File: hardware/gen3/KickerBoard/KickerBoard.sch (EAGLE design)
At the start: 109 parts, among them U2 ATMEGA165PV-8AU

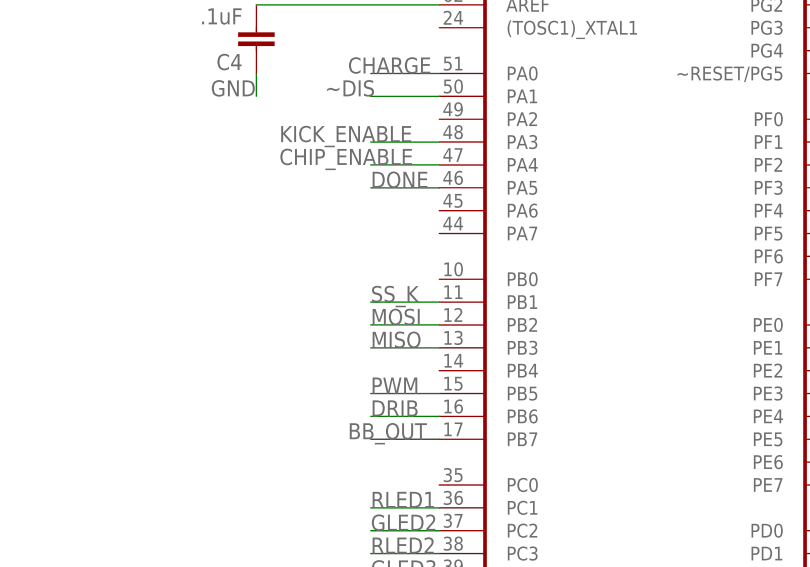
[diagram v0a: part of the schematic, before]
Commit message: fixed slave select issues
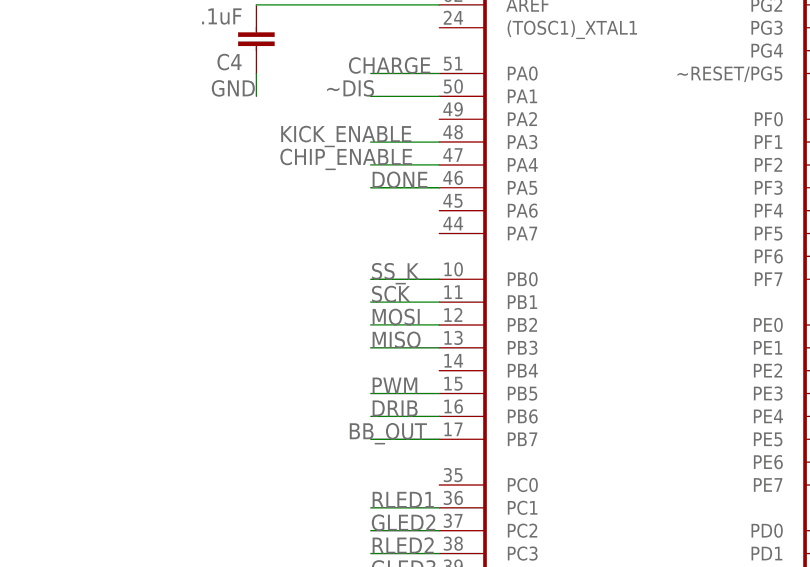
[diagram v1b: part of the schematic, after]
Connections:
- net SCK: now also U2.PB1
- net SS_K: now also U2.PB0; no longer U2.PB1
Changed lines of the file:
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@@
 <?xml version="1.0" encoding="utf-8"?>
 <!DOCTYPE eagle SYSTEM "eagle.dtd">
-<eagle version="6.4">
+<eagle version="7.2.0">
 <drawing>
 <settings>
@@
 <grid distance="0.1" unitdist="inch" unit="inch" style="lines" multiple="1" display="no" altdistance="0.01" altunitdist="inch" altunit="inch"/>
 <layers>
-<layer number="1" name="Top" color="4" fill="1" visible="yes" active="no"/>
-<layer number="2" name="Route2" color="1" fill="3" visible="yes" active="no"/>
-<layer number="3" name="Route3" color="4" fill="3" visible="yes" active="no"/>
-<layer number="14" name="Route14" color="1" fill="6" visible="yes" active="no"/>
-<layer number="15" name="Route15" color="4" fill="6" visible="yes" active="no"/>
-<layer number="16" name="Bottom" color="1" fill="1" visible="yes" active="no"/>
-<layer number="17" name="Pads" color="2" fill="1" visible="yes" active="no"/>
-<layer number="18" name="Vias" color="2" fill="1" visible="yes" active="no"/>
-<layer number="19" name="Unrouted" color="6" fill="1" visible="yes" active="no"/>
-<layer number="20" name="Dimension" color="15" fill="1" visible="yes" active="no"/>
-<layer number="21" name="tPlace" color="16" fill="1" visible="yes" active="no"/>
-<layer number="22" name="bPlace" color="14" fill="1" visible="yes" active="no"/>
-<layer number="23" name="tOrigins" color="15" fill="1" visible="yes" active="no"/>
-<layer number="24" name="bOrigins" color="15" fill="1" visible="yes" active="no"/>
-<layer number="25" name="tNames" color="7" fill="1" visible="yes" active="no"/>
-<layer number="26" name="bNames" color="7" fill="1" visible="yes" active="no"/>
-<layer number="27" name="tValues" color="7" fill="1" visible="yes" active="no"/>
-<layer number="28" name="bValues" color="7" fill="1" visible="yes" active="no"/>
+<layer number="1" name="Top" color="4" fill="1" visible="no" active="no"/>
+<layer number="2" name="Route2" color="1" fill="3" visible="no" active="no"/>
+<layer number="3" name="Route3" color="4" fill="3" visible="no" active="no"/>
+<layer number="14" name="Route14" color="1" fill="6" visible="no" active="no"/>
+<layer number="15" name="Route15" color="4" fill="6" visible="no" active="no"/>
+<layer number="16" name="Bottom" color="1" fill="1" visible="no" active="no"/>
+<layer number="17" name="Pads" color="2" fill="1" visible="no" active="no"/>
+<layer number="18" name="Vias" color="2" fill="1" visible="no" active="no"/>
+<layer number="19" name="Unrouted" color="6" fill="1" visible="no" active="no"/>
+<layer number="20" name="Dimension" color="15" fill="1" visible="no" active="no"/>
+<layer number="21" name="tPlace" color="16" fill="1" visible="no" active="no"/>
+<layer number="22" name="bPlace" color="14" fill="1" visible="no" active="no"/>
+<layer number="23" name="tOrigins" color="15" fill="1" visible="no" active="no"/>
+<layer number="24" name="bOrigins" color="15" fill="1" visible="no" active="no"/>
+<layer number="25" name="tNames" color="7" fill="1" visible="no" active="no"/>
+<layer number="26" name="bNames" color="7" fill="1" visible="no" active="no"/>
+<layer number="27" name="tValues" color="7" fill="1" visible="no" active="no"/>
+<layer number="28" name="bValues" color="7" fill="1" visible="no" active="no"/>
 <layer number="29" name="tStop" color="7" fill="3" visible="no" active="no"/>
 <layer number="30" name="bStop" color="7" fill="6" visible="no" active="no"/>
@@
 <layer number="35" name="tGlue" color="7" fill="4" visible="no" active="no"/>
 <layer number="36" name="bGlue" color="7" fill="5" visible="no" active="no"/>
-<layer number="37" name="tTest" color="7" fill="1" visible="yes" active="no"/>
-<layer number="38" name="bTest" color="7" fill="1" visible="yes" active="no"/>
+<layer number="37" name="tTest" color="7" fill="1" visible="no" active="no"/>
+<layer number="38" name="bTest" color="7" fill="1" visible="no" active="no"/>
 <layer number="39" name="tKeepout" color="4" fill="11" visible="no" active="no"/>
 <layer number="40" name="bKeepout" color="1" fill="11" visible="no" active="no"/>
@@
 <layer number="44" name="Drills" color="7" fill="1" visible="no" active="no"/>
 <layer number="45" name="Holes" color="7" fill="1" visible="no" active="no"/>
-<layer number="46" name="Milling" color="3" fill="1" visible="yes" active="no"/>
-<layer number="47" name="Measures" color="7" fill="1" visible="yes" active="no"/>
-<layer number="48" name="Document" color="7" fill="1" visible="yes" active="no"/>
-<layer number="49" name="Reference" color="7" fill="1" visible="yes" active="no"/>
-<layer number="50" name="dxf" color="7" fill="1" visible="yes" active="no"/>
-<layer number="51" name="tDocu" color="6" fill="1" visible="yes" active="no"/>
-<layer number="52" name="bDocu" color="7" fill="1" visible="yes" active="no"/>
-<layer number="53" name="tGND_GNDA" color="7" fill="9" visible="yes" active="no"/>
-<layer number="54" name="bGND_GNDA" color="1" fill="9" visible="yes" active="no"/>
-<layer number="56" name="wert" color="7" fill="1" visible="yes" active="no"/>
-<layer number="57" name="tCAD" color="7" fill="1" visible="yes" active="no"/>
-<layer number="59" name="tCarbon" color="7" fill="1" visible="yes" active="no"/>
-<layer number="60" name="bCarbon" color="7" fill="1" visible="yes" active="no"/>
+<layer number="46" name="Milling" color="3" fill="1" visible="no" active="no"/>
+<layer number="47" name="Measures" color="7" fill="1" visible="no" active="no"/>
+<layer number="48" name="Document" color="7" fill="1" visible="no" active="no"/>
+<layer number="49" name="Reference" color="7" fill="1" visible="no" active="no"/>
+<layer number="50" name="dxf" color="7" fill="1" visible="no" active="no"/>
+<layer number="51" name="tDocu" color="6" fill="1" visible="no" active="no"/>
+<layer number="52" name="bDocu" color="7" fill="1" visible="no" active="no"/>
+<layer number="53" name="tGND_GNDA" color="7" fill="9" visible="no" active="no"/>
+<layer number="54" name="bGND_GNDA" color="1" fill="9" visible="no" active="no"/>
+<layer number="56" name="wert" color="7" fill="1" visible="no" active="no"/>
+<layer number="57" name="tCAD" color="7" fill="1" visible="no" active="no"/>
+<layer number="59" name="tCarbon" color="7" fill="1" visible="no" active="no"/>
+<layer number="60" name="bCarbon" color="7" fill="1" visible="no" active="no"/>
 <layer number="90" name="Modules" color="5" fill="1" visible="yes" active="yes"/>
 <layer number="91" name="Nets" color="2" fill="1" visible="yes" active="yes"/>
@@
 <label x="55.88" y="35.56" size="1.778" layer="95"/>
 </segment>
+<segment>
+<pinref part="U2" gate="A" pin="PB1"/>
+<wire x1="101.6" y1="114.3" x2="93.98" y2="114.3" width="0.1524" layer="91"/>
+<label x="93.98" y="114.3" size="1.778" layer="95"/>
+</segment>
 </net>
 <net name="SS_M" class="0">
@@
 </segment>
 <segment>
-<pinref part="U2" gate="A" pin="PB1"/>
-<wire x1="101.6" y1="114.3" x2="93.98" y2="114.3" width="0.1524" layer="91"/>
-<label x="93.98" y="114.3" size="1.778" layer="95"/>
+<pinref part="U2" gate="A" pin="PB0"/>
+<wire x1="101.6" y1="116.84" x2="93.98" y2="116.84" width="0.1524" layer="91"/>
+<label x="93.98" y="116.84" size="1.778" layer="95"/>
 </segment>
 </net>

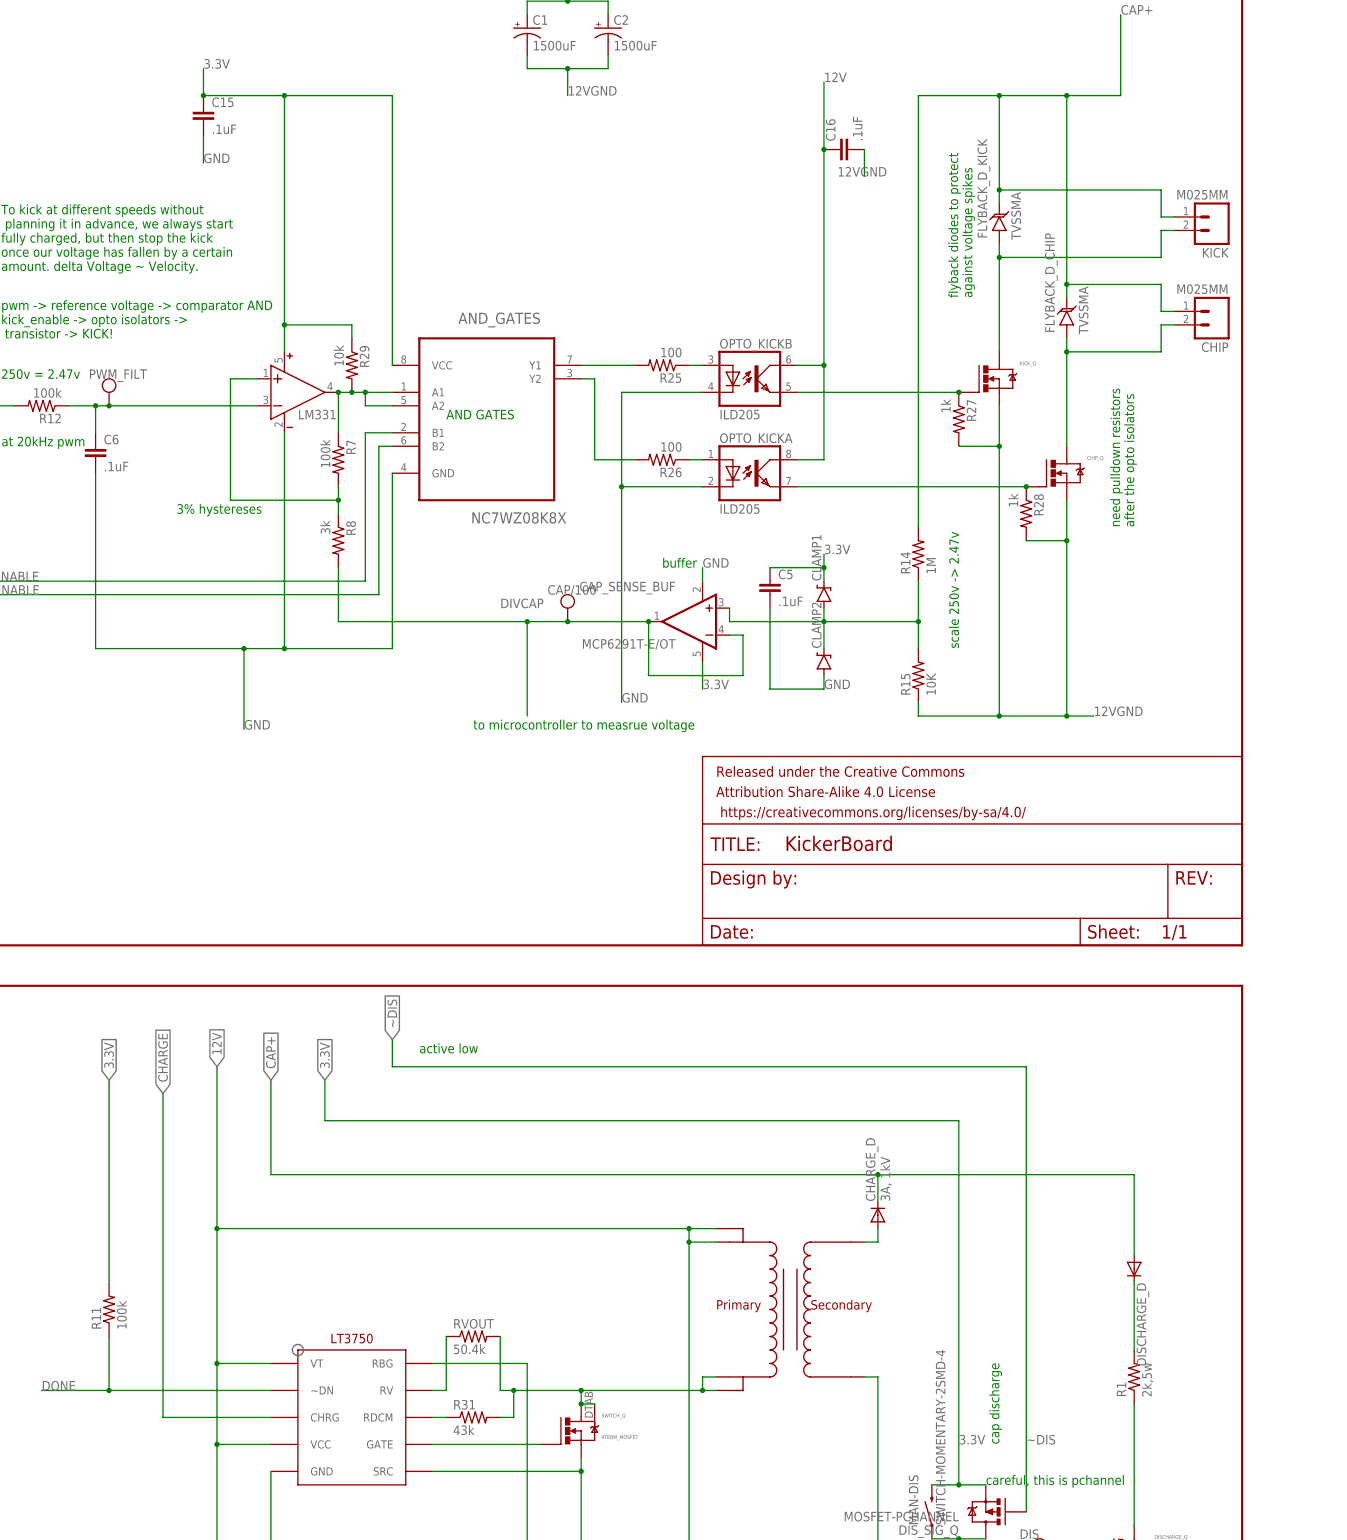
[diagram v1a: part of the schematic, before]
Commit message: parts for kicker
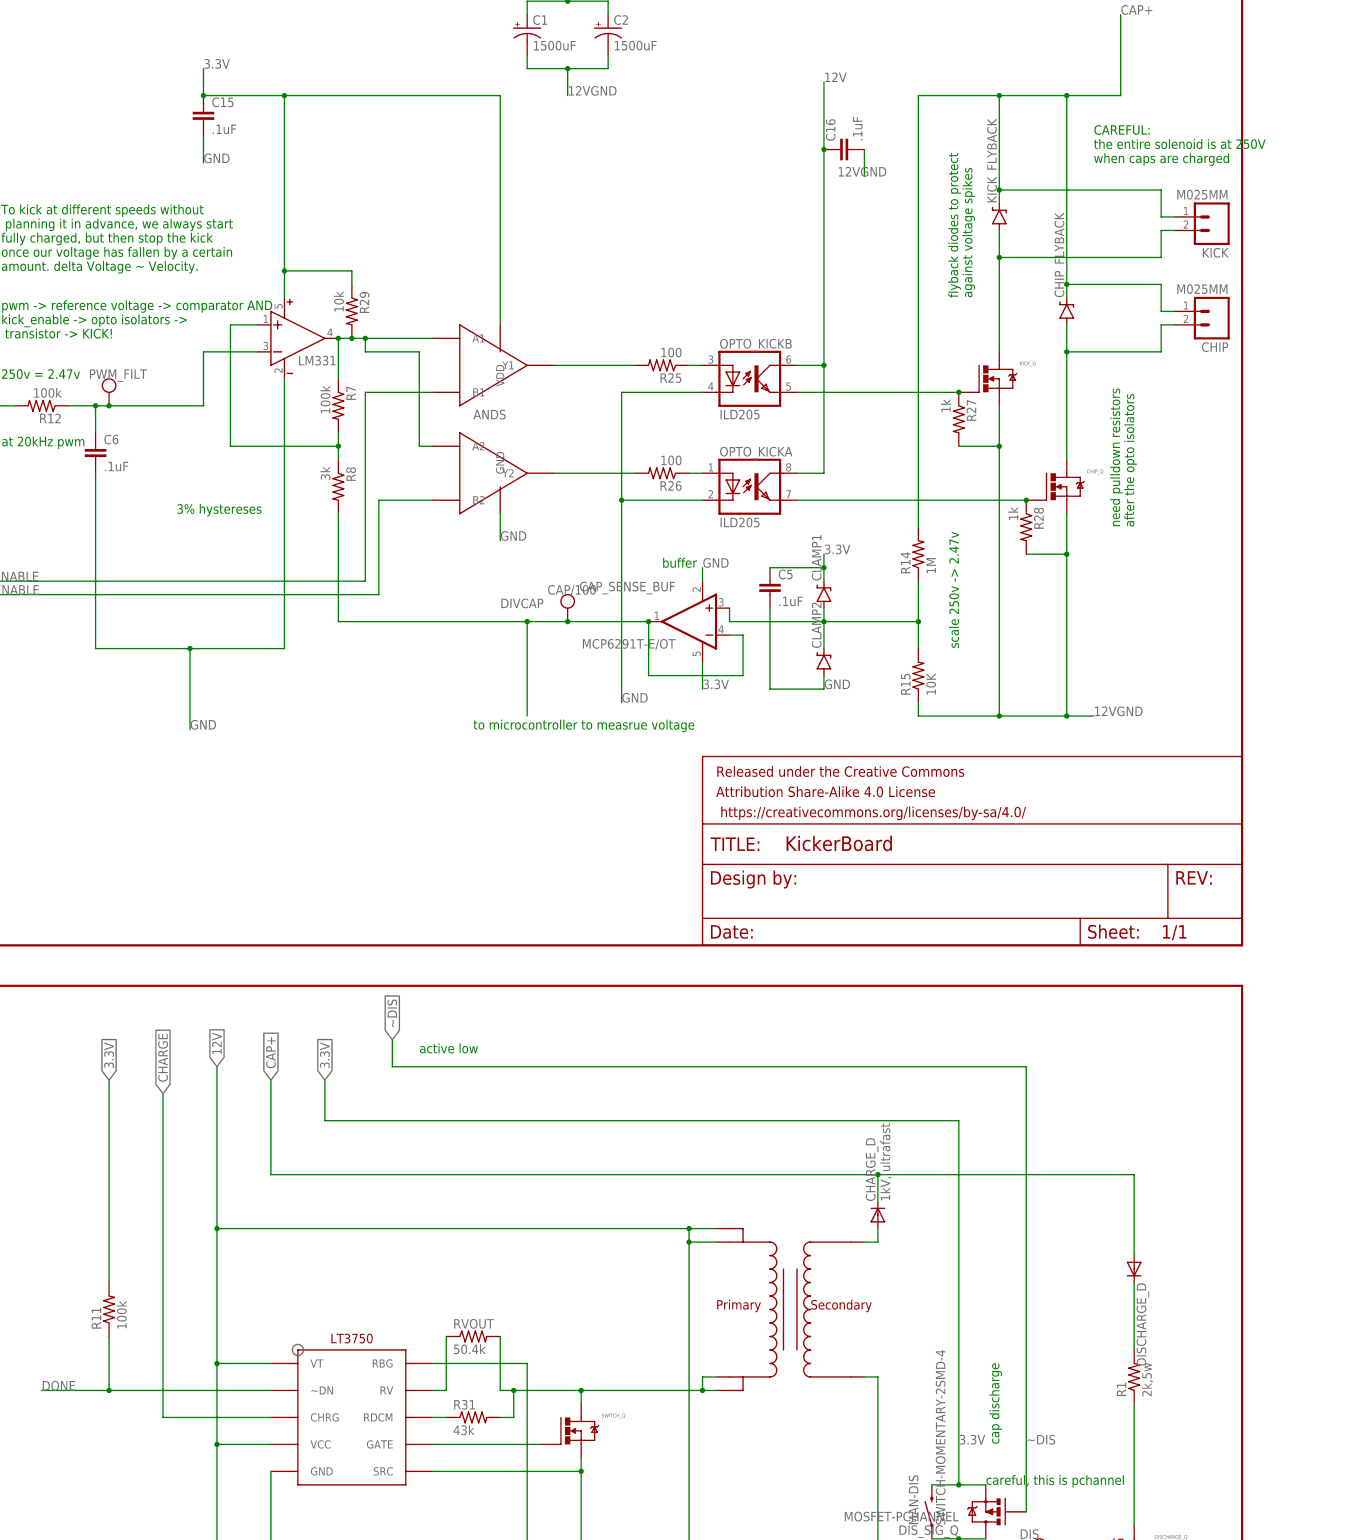
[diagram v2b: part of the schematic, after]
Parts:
- removed AND_GATES: NC7WZ08K8X, Fairchild_By_element14_Batch_1:NC7WZ08K8X
- removed FLYBACK_D_CHIP, FLYBACK_D_KICK: TVSSMA, SparkFun-DiscreteSemi:TVSSMA
- added ANDS: AND-DUAL, gen3:AND-DUAL
- added CHIP_FLYBACK, KICK_FLYBACK: DIODE-ZENERDO214AB, gen3:DIODE-ZENERDO214AB
- CHARGE_D: value 3A, 1kV -> 1kV, ultrafast; device gen3:DIODE-DO214AA -> gen3:DIODE-DO214AC
- CLAMP1, CLAMP2: value DIODE-ZENERDO214BA -> DIODE-ZENERDO214AC; device gen3:DIODE-ZENERDO214BA -> gen3:DIODE-ZENERDO214AC
- SWITCH_Q: value 4TERM_MOSFET -> (none); device gen3:4TERM_MOSFET -> gen3:N-MOSFETDPAK
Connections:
- net 3.3V: now also ANDS.VDD; no longer AND_GATES.VCC
- net AND_CHIP: now also ANDS.Y2; no longer AND_GATES.Y2
- net AND_KICK: now also ANDS.Y1; no longer AND_GATES.Y1
- net CAP+: now also CHIP_FLYBACK.C, KICK_FLYBACK.C; no longer FLYBACK_D_CHIP.C, FLYBACK_D_KICK.C
- net CHIP_ENABLE: now also ANDS.B2; no longer AND_GATES.B2
- net COMP_OUT: now also ANDS.A1, ANDS.A2; no longer AND_GATES.A1, AND_GATES.A2
- net GND: now also ANDS.GND; no longer AND_GATES.GND
- net KICK_ENABLE: now also ANDS.B1; no longer AND_GATES.B1
- net N$33: now also KICK_FLYBACK.A; no longer FLYBACK_D_KICK.A
- net N$34: now also CHIP_FLYBACK.A; no longer FLYBACK_D_CHIP.A
- net N$5: no longer SWITCH_Q.D2
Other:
- note added: "CAREFUL: the entire solenoid is at 250V when caps are charged"
- note removed: "AND GATES"
- moved on the sheet: CHIP_Q, OPTO_KICKA, R26, R28, R29, R7, R8
